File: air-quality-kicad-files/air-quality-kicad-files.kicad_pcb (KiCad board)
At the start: 2 copper layers, 77 x 39.5 mm, 11 parts, among them U2 XIAO-ESP32C3

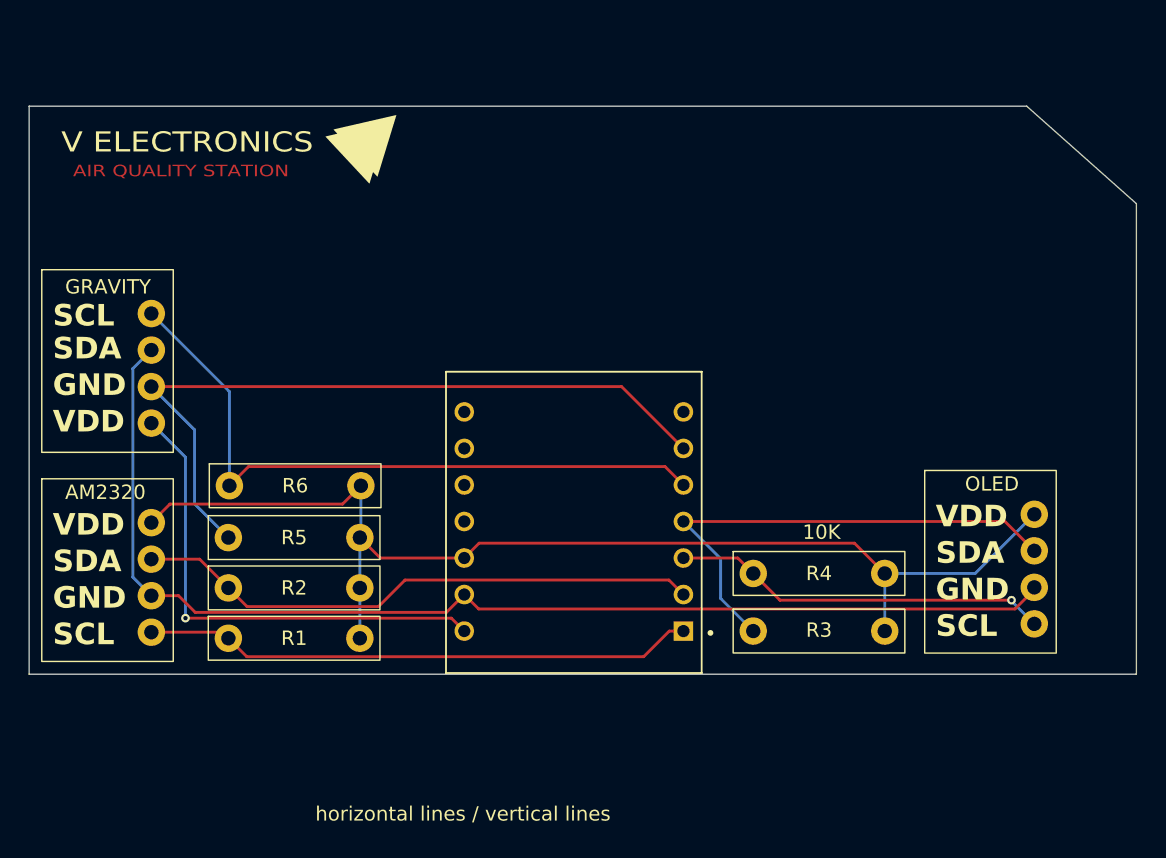
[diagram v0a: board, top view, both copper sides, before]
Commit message: added resistors, buzzer circuit, holes, cleaned up files
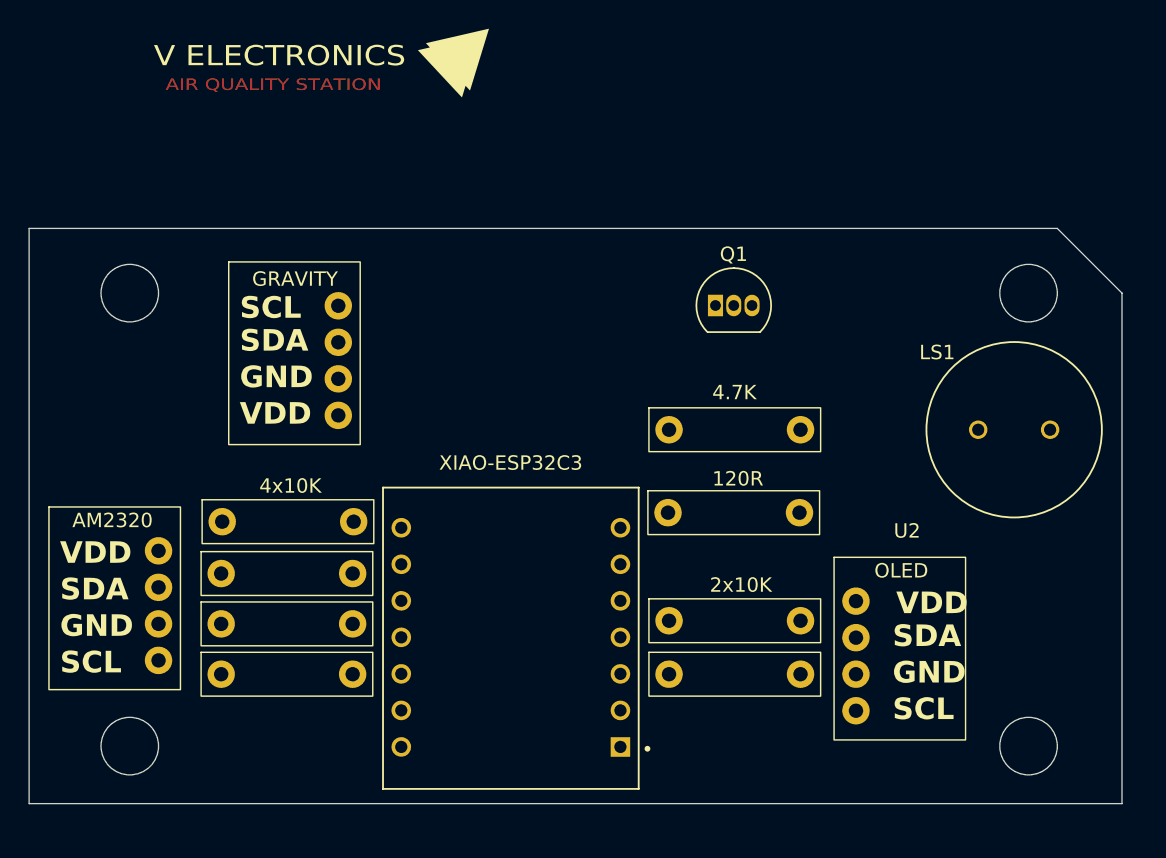
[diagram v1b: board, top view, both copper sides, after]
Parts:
- added LS1: PS1240P02BT, footprints:buzzer-XDCR_PS1240P02BT, F.Cu at (176.0, 103.5)
- added Q1: 2N3904, Package_TO_SOT_THT:TO-92_Inline, F.Cu at (155.2, 94.9)
- added R7: ~, footprints:120R, F.Cu at (156.5, 102.4)
- added R8: ~, footprints:4-7K, F.Cu at (156.8, 95.9)
- U2: value XIAO-ESP32C3 -> ~; footprint footprints:XIAO-ESP32C3 -> footprints:OLED
- U4: value ~ -> XIAO-ESP32C3; footprint footprints:OLED -> footprints:XIAO-ESP32C3
- moved U4 37.4 mm to (141.0, 118.0), turned to 180 degrees
- moved U2 23.3 mm to (168.6, 108.1), turned to 0 degrees
- moved U3 13.0 mm to (126.2, 87.8)
- moved G*** 8.80 mm to (137.0, 78.0)
- moved R4 6.72 mm to (156.8, 109.7)
- moved R3 6.58 mm to (156.8, 113.4)
- moved R1 2.55 mm to (125.7, 106.4)
- moved R2 2.55 mm to (125.8, 102.8)
- moved R5 2.55 mm to (125.7, 109.9)
- moved R6 2.55 mm to (125.7, 113.4)
- moved U1 2.02 mm to (113.5, 103.5)
- renumbered R5 to R1, R6 to R2, R2 to R5, R1 to R6
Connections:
- R1 pad 1: Net-(U2-D5) -> Net-(U3-SDA)
- R2 pad 1: Net-(U2-D4) -> Net-(U3-SCL)
- R3 pad 1: Net-(U2-D3) -> Net-(U2-SDA)
- R4 pad 1: Net-(U2-D2) -> Net-(U2-SCL)
- U2 pad 1: Net-(U1-SCL) -> 3.3V
- U2 pad 2: Net-(U1-SDA) -> Net-(U2-SDA)
- U2 pad 3: Net-(U2-D2) -> GND
- U2 pad 4: Net-(U2-D3) -> Net-(U2-SCL)
- U3 pad 2: Net-(U2-D5) -> Net-(U3-SDA)
- U3 pad 4: Net-(U2-D4) -> Net-(U3-SCL)
- U4 pad 1: 3.3V -> Net-(U1-SCL)
- U4 pad 2: Net-(U2-D3) -> Net-(U1-SDA)
- U4 pad 3: GND -> Net-(U2-SCL)
- U4 pad 4: Net-(U2-D2) -> Net-(U2-SDA)
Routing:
- net GND: track 81.7 -> 0.00 mm
- net 3.3V: track 80.8 -> 0.00 mm
- net Net-(U2-D5): track 51.5 -> 0.00 mm
- net Net-(U2-D4): track 46.9 -> 0.00 mm
- net Net-(U1-SDA): track 39.6 -> 0.00 mm
- net Net-(U1-SCL): track 38.4 -> 0.00 mm
- net Net-(U2-D3): track 34.9 -> 0.00 mm
- net 5VUSB: track 34.3 -> 0.00 mm, vias 1 -> 0
- net Net-(U2-D2): track 26.3 -> 0.00 mm, vias 1 -> 0
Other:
- board size 77 x 39.5 mm -> 76 x 40 mm
- board text added: "2x10K"
- board text added: "4x10K"
- board text removed: "horizontal lines / vertical lines"
